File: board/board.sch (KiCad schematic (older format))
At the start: 34 parts, among them P2 POWER, P3 JTAG, U3 LFSPXO025560

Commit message: Schematics and Start of Board Layout
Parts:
- removed C36, C37, C38, C39, C40, C41, C42, C43: 100nF, Capacitors_SMD:C_0805_HandSoldering, symbol C_Small
- removed P3: JTAG, Pin_Headers:Pin_Header_Straight_2x05_Pitch2.54mm, symbol CONN_02X05
- removed U3: LFSPXO025560, Crystals:Crystal_SMD_EuroQuartz_MT-4pin_3.2x2.5mm_HandSoldering, symbol LFSPXO025560
- added AMP1: THS7316, Housings_SOIC:SOIC-8_3.9x4.9mm_Pitch1.27mm, symbol THS7316
- added C1, C2, C3, C4, C5: 10uF, Capacitors_SMD:C_0805_HandSoldering, symbol C_Small
- added GPIO1: CONN_02X17, Pin_Headers:Pin_Header_Straight_2x17_Pitch2.54mm, symbol CONN_02X17
- added JTAG1: CONN_02X05, Pin_Headers:Pin_Header_Straight_2x05_Pitch2.54mm, symbol CONN_02X05
- added L1, L2: 10mH, Capacitors_SMD:C_0805_HandSoldering, symbol L_Small
- added OSC1: XO32050UITA, Oscillators:Oscillator_SMD_EuroQuartz_XO32-4pin_3.2x2.5mm_HandSoldering, symbol XO32050UITA
- added R1, R12, R19: 1k, Resistors_SMD:R_0805_HandSoldering, symbol R_Small
- added R10, R11, R14, R24, R25, R26, R9: 10k, Resistors_SMD:R_0805_HandSoldering, symbol R_Small
- added R13, R20, R3: 2k, Resistors_SMD:R_0805_HandSoldering, symbol R_Small
- added R15, R21, R4: 4k, Resistors_SMD:R_0805_HandSoldering, symbol R_Small
- added R16, R22, R5: 8k, Resistors_SMD:R_0805_HandSoldering, symbol R_Small
- added R17, R23, R6: 16k, Resistors_SMD:R_0805_HandSoldering, symbol R_Small
- added R18, R8: 150, Resistors_SMD:R_0805_HandSoldering, symbol R_Small
- added R27, R28, R29: 75, Resistors_SMD:R_0805_HandSoldering, symbol R_Small
- added R7: 1k1, Resistors_SMD:R_0805_HandSoldering, symbol R_Small
- added RCA1: TrippleRCA, footprints:TrippleRCA, symbol TrippleRCA
- added REG1: LM1117IMPX-3.3, TO_SOT_Packages_SMD:SOT-223, symbol LM1117IMPX-3.3
- C7: value 47u -> 100nF; footprint Capacitors_SMD:C_1206_HandSoldering -> Capacitors_SMD:C_0805_HandSoldering
- POWER1: renamed from P2; value POWER -> CONM_01x02
- R2: value 10k -> 150
- U2: renamed from U?; footprint (none) -> footprints:QFP_144_GND
- renumbered C17 to C11, C18 to C12, C19 to C13, C20 to C14, C21 to C15, C22 to C16, C23 to C17, C24 to C18, C25 to C19, C26 to C20, C27 to C21, C28 to C22, C29 to C23, C30 to C24, C35 to C25, C13 to C6
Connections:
- net labels removed: +5V, 1V8A, 1V8B, 1V8C
- wire segments 87 -> 376
- no-connect marks 3 -> 44
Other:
- note added: "PB"
- note added: "PR"
- note added: "Y"
- moved on the sheet: C6, POWER1, U2

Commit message: Board layout finished
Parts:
- removed GPIO1: CONN_02X17, Pin_Headers:Pin_Header_Straight_2x17_Pitch2.54mm, symbol CONN_02X17
- added C26, C27, C28, C29, C30: 100nF, Capacitors_SMD:C_0603_HandSoldering, symbol C_Small
- added C8: 10uF, Capacitors_SMD:C_0805_HandSoldering, symbol C_Small
- added GPIO1: CONN_02X08, Pin_Headers:Pin_Header_Straight_2x08_Pitch2.54mm, symbol CONN_02X08
- added GPIO2: CONN_02X05, Pin_Headers:Pin_Header_Straight_2x05_Pitch2.54mm, symbol CONN_02X05
- C11, C12, C13, C14, C15, C16, C17, C18, C19, C20, C21, C22, C23, C24, C25, C31, C32, C33, C34, C6, C7: footprint Capacitors_SMD:C_0805_HandSoldering -> Capacitors_SMD:C_0603_HandSoldering
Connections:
- net 3V3A: now also C5.2, C8.2, GPIO1.2 (P2), GPIO2.2 (P2); no longer C5.1, REG1.2 (OUT)
- net 3V3B: now also C26.1, C27.1, C28.1, C29.1, C30.1
- net GND: now also C5.1, C26.2, C27.2, C28.2, C29.2, C30.2, C8.1, GPIO1.1 (P1), GPIO2.1 (P1); no longer C5.2
- net at U2.100 (IO_6): no longer R19.1
- net at U2.101 (IO_6): no longer R20.1
- net at U2.103 (IO_6): no longer R21.1
- net at U2.105 (IO_6): no longer R22.1
- net at U2.106 (IO_6): no longer R23.1
- net at U2.24 (IO_1B): now also GPIO2.3 (P3)
- net at U2.25 (IO_2/CLK0n): now also GPIO2.4 (P4); no longer OSC1.3 (OUT)
- net at U2.26 (IO_2/CLK0p): now also GPIO2.5 (P5)
- net at U2.27 (IO_2/CLK1n): now also GPIO2.6 (P6)
- net at U2.28 (IO_2/CLK1p): now also GPIO2.7 (P7)
- net at U2.31 (IO_2): now also GPIO2.8 (P8)
- net at U2.32 (IO_2/PLL_L_CLKOUTn): now also GPIO2.9 (P9)
- net at U2.33 (IO_2/PLL_L_CLKOUTp): now also GPIO2.10 (P10)
- net at U2.39 (IO_3): now also R1.1
- net at U2.40 (IO_3): now also R3.1
- net at U2.41 (IO_3): now also R4.1
- net at U2.42 (IO_3): now also R5.1
- net at U2.44 (IO_3): now also R6.1
- net at U2.46 (IO_3): now also R7.1
- net at U2.47 (IO_3): now also R12.1
- net at U2.48 (IO_3): now also R13.1
- net at U2.61 (IO_3): now also R15.1
- net at U2.62 (IO_3): now also R16.1
- net at U2.63 (IO_3): now also R17.1
- net at U2.65 (IO_3): now also R19.1
- net at U2.67 (IO_3): now also R20.1
- net at U2.68 (IO_3): now also R21.1
- net at U2.69 (IO_3): now also R22.1
- net at U2.70 (IO_3): now also R23.1
- net at U2.74 (IO_5): now also GPIO1.16 (P16)
- net at U2.75 (IO_5): now also GPIO1.15 (P15)
- net at U2.76 (IO_5): now also GPIO1.14 (P14)
- net at U2.77 (IO_5): now also GPIO1.13 (P13)
- net at U2.78 (IO_5): now also GPIO1.12 (P12); no longer R1.1
- net at U2.79 (IO_5): now also GPIO1.11 (P11); no longer R3.1
- net at U2.80 (IO_5): now also GPIO1.10 (P10)
- net at U2.81 (IO_5): now also GPIO1.9 (P9); no longer R4.1
- net at U2.84 (IO_5): now also GPIO1.8 (P8)
- net at U2.85 (IO_5): now also GPIO1.7 (P7); no longer R5.1
- net at U2.86 (IO_5): now also GPIO1.6 (P6)
- net at U2.87 (IO_5): now also GPIO1.5 (P5); no longer R6.1
- net at U2.88 (IO_6/CLK2p): now also GPIO1.4 (P4)
- net at U2.89 (IO_6/CLK2n): now also GPIO1.3 (P3); no longer R7.1
- net at U2.91 (IO_6/CLK3n): now also OSC1.3 (OUT); no longer R12.1
- net at U2.92 (IO_6): no longer R13.1
- net at U2.95 (IO_6): no longer R15.1
- net at U2.97 (IO_6): no longer R16.1
- net at U2.98 (IO_6): no longer R17.1
- no-connect marks 44 -> 55
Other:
- moved on the sheet: AMP1, C6, C7, OSC1, R1, R12, R13, R15, R16, R17, R18, R19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

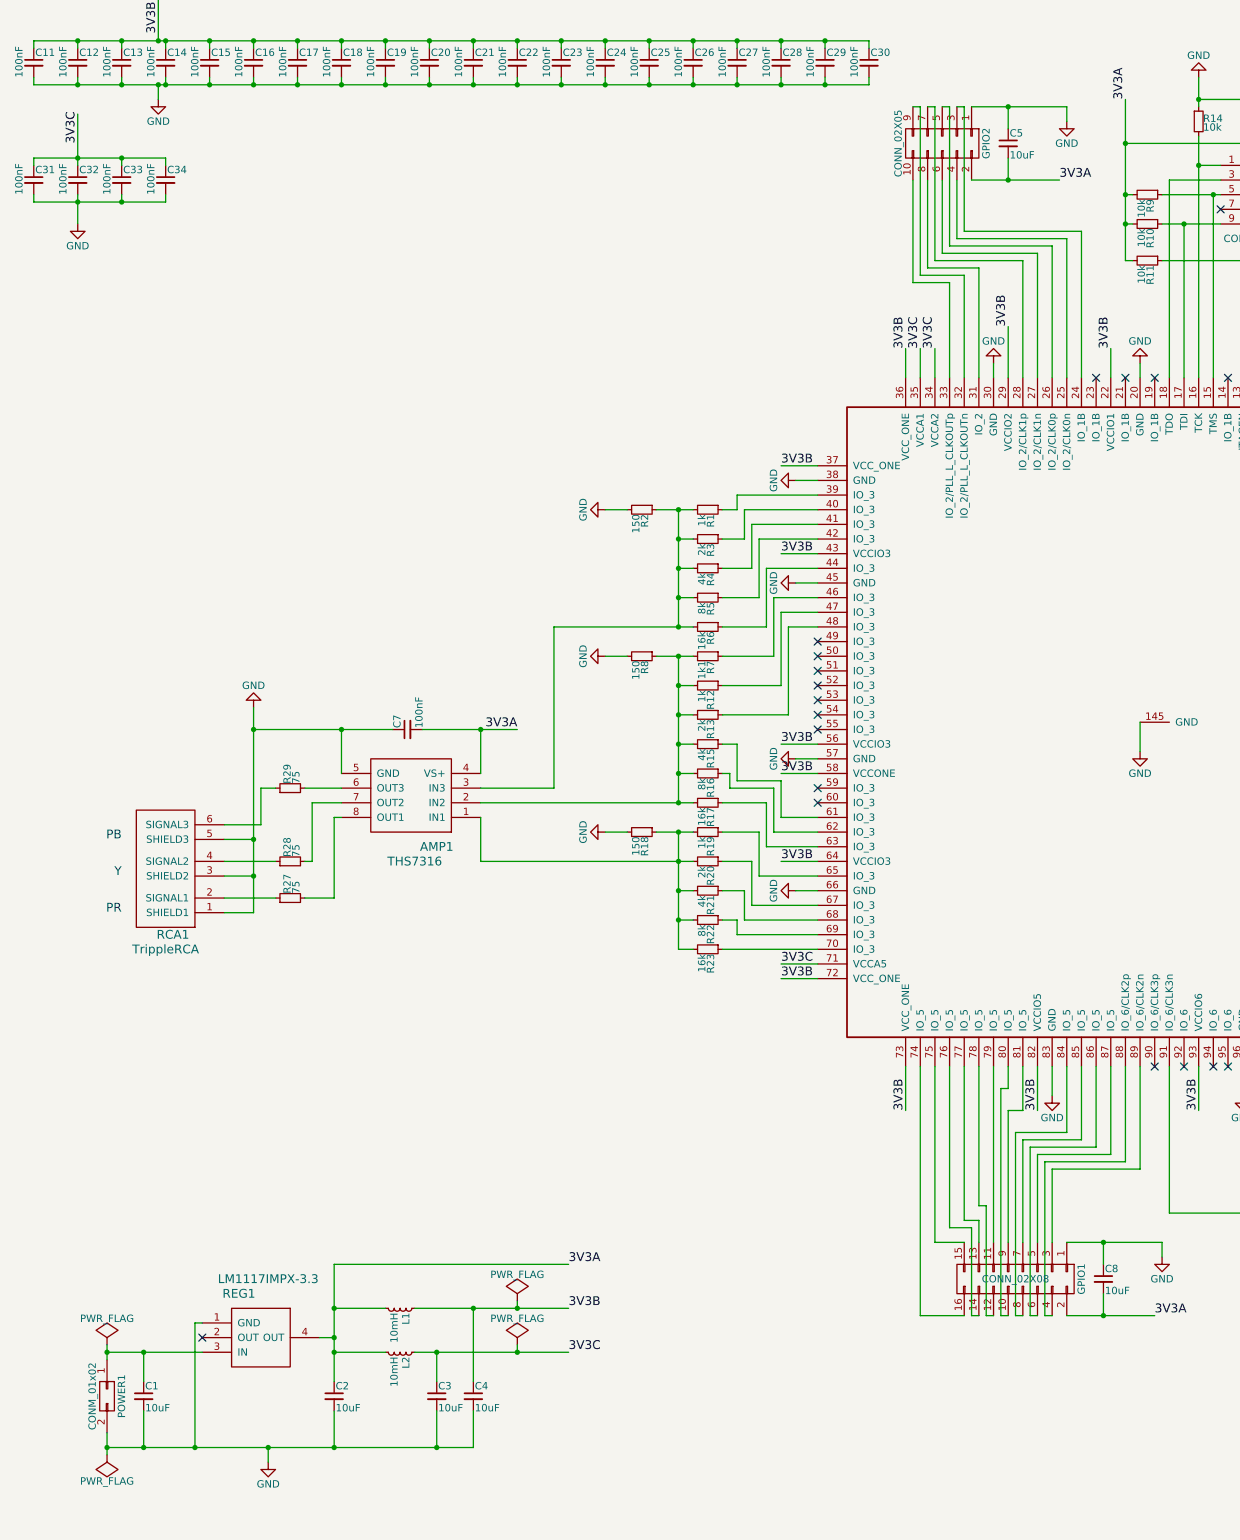
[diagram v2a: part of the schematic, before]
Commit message: Adapter board for ZX Spectrum
Plus some changes to the A-Video board itself to better fit the needs of
the ZX Spectrum mod (which currently drives the development)
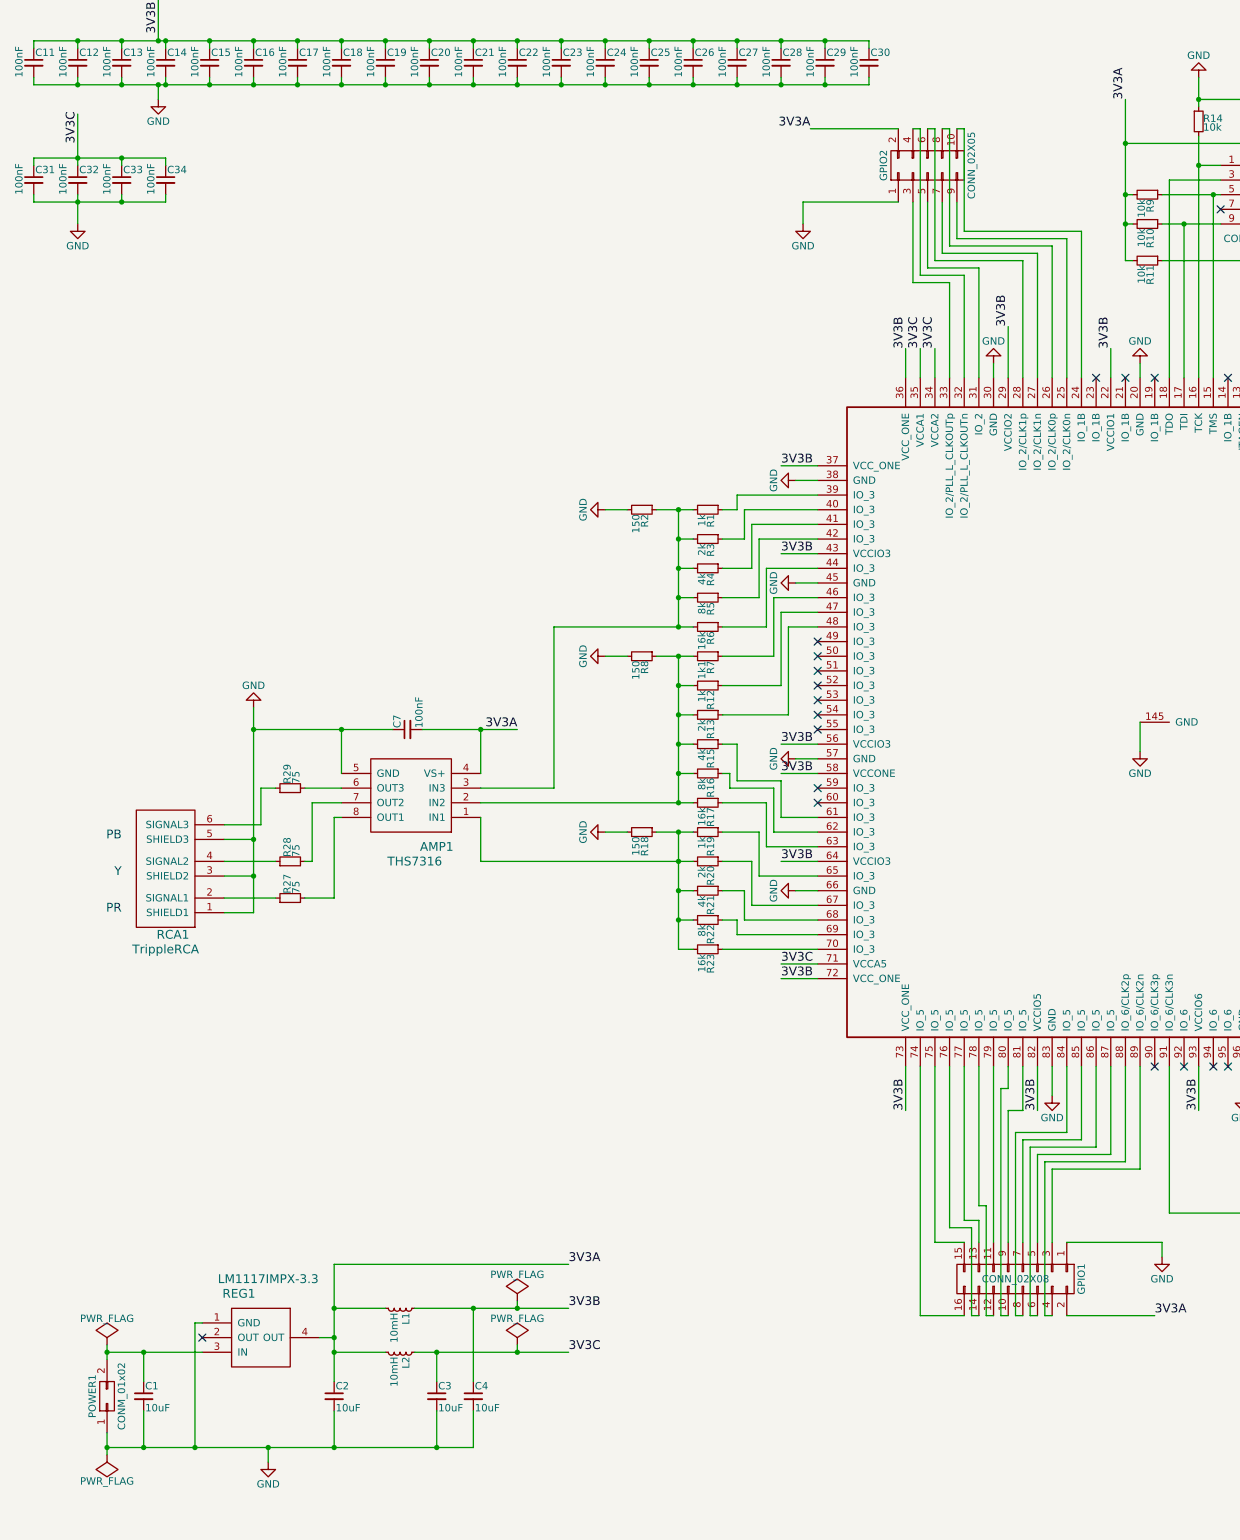
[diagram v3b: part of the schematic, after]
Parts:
- removed C5, C8: 10uF, Capacitors_SMD:C_0805_HandSoldering, symbol C_Small
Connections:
- net GND: now also POWER1.1 (P1); no longer POWER1.2 (P2)
- net at C1.1, REG1.3 (IN): now also POWER1.2 (P2); no longer POWER1.1 (P1)
- net at U2.24 (IO_1B): now also GPIO2.10 (P10); no longer GPIO2.3 (P3)
- net at U2.25 (IO_2/CLK0n): now also GPIO2.9 (P9); no longer GPIO2.4 (P4)
- net at U2.26 (IO_2/CLK0p): now also GPIO2.8 (P8); no longer GPIO2.5 (P5)
- net at U2.27 (IO_2/CLK1n): now also GPIO2.7 (P7); no longer GPIO2.6 (P6)
- net at U2.28 (IO_2/CLK1p): now also GPIO2.6 (P6); no longer GPIO2.7 (P7)
- net at U2.31 (IO_2): now also GPIO2.5 (P5); no longer GPIO2.8 (P8)
- net at U2.32 (IO_2/PLL_L_CLKOUTn): now also GPIO2.4 (P4); no longer GPIO2.9 (P9)
- net at U2.33 (IO_2/PLL_L_CLKOUTp): now also GPIO2.3 (P3); no longer GPIO2.10 (P10)
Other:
- moved on the sheet: GPIO2
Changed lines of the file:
@@
 F 3 "" H 1200 8900 50  0000 C CNN
 	1    1200 10100
-	0    1    1    0
+	0    -1   -1   0
 $EndComp
 $Comp
@@
 	0    1    1    0
 $EndComp
-$Comp
-L C_Small C8
-U 1 1 59EB0B1F
-P 8000 9300
-F 0 "C8" H 8010 9370 50  0000 L CNN
-F 1 "10uF" H 8010 9220 50  0000 L CNN
-F 2 "Capacitors_SMD:C_0805_HandSoldering" H 8000 9300 50  0001 C CNN
-F 3 "" H 8000 9300 50  0000 C CNN
-	1    8000 9300
-	1    0    0    -1
-$EndComp
 Text Label 8350 9550 0    60   ~ 0
 3V3A
@@
 	7750 9050 8400 9050
 Wire Wire Line
-	8000 9200 8000 9050
-Connection ~ 8000 9050
-Wire Wire Line
 	7750 9550 8350 9550
 Wire Wire Line
 	8400 9050 8400 9150
-Wire Wire Line
-	8000 9400 8000 9550
-Connection ~ 8000 9550
 Wire Wire Line
 	6750 9550 7050 9550
@@
 L CONN_02X05 GPIO2
 U 1 1 59EBB195
-P 6900 1550
-F 0 "GPIO2" H 6900 1850 50  0000 C CNN
-F 1 "CONN_02X05" H 6900 1250 50  0000 C CNN
-F 2 "Pin_Headers:Pin_Header_Straight_2x05_Pitch2.54mm" H 6900 350 50  0001 C CNN
-F 3 "" H 6900 350 50  0000 C CNN
-	1    6900 1550
-	0    1    1    0
+P 6800 1700
+F 0 "GPIO2" H 6800 2000 50  0000 C CNN
+F 1 "CONN_02X05" H 6800 1400 50  0000 C CNN
+F 2 "Pin_Headers:Pin_Header_Straight_2x05_Pitch2.54mm" H 6800 500 50  0001 C CNN
+F 3 "" H 6800 500 50  0000 C CNN
+	1    6800 1700
+	0    -1   -1   0
 $EndComp
 NoConn ~ 8350 7850
@@
 NoConn ~ 9850 7850
 NoConn ~ 9950 7850
-$Comp
-L C_Small C5
-U 1 1 59EC1E6D
-P 7350 1550
-F 0 "C5" H 7360 1620 50  0000 L CNN
-F 1 "10uF" H 7360 1470 50  0000 L CNN
-F 2 "Capacitors_SMD:C_0805_HandSoldering" H 7350 1550 50  0001 C CNN
-F 3 "" H 7350 1550 50  0000 C CNN
-	1    7350 1550
-	1    0    0    -1
-$EndComp
-Text Label 7700 1800 0    60   ~ 0
+Text Label 6000 1450 2    60   ~ 0
 3V3A
 $Comp
 L GND #PWR031
 U 1 1 59EC1E74
-P 7750 1400
-F 0 "#PWR031" H 7750 1150 50  0001 C CNN
-F 1 "GND" H 7750 1250 50  0000 C CNN
-F 2 "" H 7750 1400 50  0000 C CNN
-F 3 "" H 7750 1400 50  0000 C CNN
-	1    7750 1400
-	1    0    0    -1
-$EndComp
-Wire Wire Line
-	7100 1300 7750 1300
-Wire Wire Line
-	7350 1450 7350 1300
-Connection ~ 7350 1300
-Wire Wire Line
-	7100 1800 7700 1800
-Wire Wire Line
-	7750 1300 7750 1400
-Wire Wire Line
-	7350 1650 7350 1800
-Connection ~ 7350 1800
+P 5950 2100
+F 0 "#PWR031" H 5950 1850 50  0001 C CNN
+F 1 "GND" H 5950 1950 50  0000 C CNN
+F 2 "" H 5950 2100 50  0000 C CNN
+F 3 "" H 5950 2100 50  0000 C CNN
+	1    5950 2100
+	1    0    0    -1
+$EndComp
+Wire Wire Line
+	5950 1950 6600 1950
+Wire Wire Line
+	6000 1450 6600 1450
 Wire Wire Line
 	6950 2500 6700 2500
 Wire Wire Line
-	6700 2500 6700 1800
+	6700 2500 6700 1950
 Wire Wire Line
 	7050 2450 6750 2450
 Wire Wire Line
-	6750 2450 6750 1300
-Wire Wire Line
-	6750 1300 6700 1300
+	6750 2450 6750 1450
+Wire Wire Line
+	6750 1450 6700 1450
 Wire Wire Line
 	7150 3150 7150 2400
@@
 	7150 2400 6800 2400
 Wire Wire Line
-	6800 2400 6800 1800
+	6800 2400 6800 1950
 Wire Wire Line
 	7450 2350 6850 2350
 Wire Wire Line
-	6850 2350 6850 1300
-Wire Wire Line
-	6850 1300 6800 1300
+	6850 2350 6850 1450
+Wire Wire Line
+	6850 1450 6800 1450
 Wire Wire Line
 	7550 2300 6900 2300
 Wire Wire Line
-	6900 2300 6900 1800
+	6900 2300 6900 1950
 Wire Wire Line
 	7650 3150 7650 2250
@@
 	7650 2250 6950 2250
 Wire Wire Line
-	6950 2250 6950 1300
-Wire Wire Line
-	6950 1300 6900 1300
+	6950 2250 6950 1450
+Wire Wire Line
+	6950 1450 6900 1450
 Wire Wire Line
 	7750 3150 7750 2200
@@
 	7750 2200 7000 2200
 Wire Wire Line
-	7000 2200 7000 1800
+	7000 2200 7000 1950
 Wire Wire Line
 	7850 3150 7850 2150
@@
 	7850 2150 7050 2150
 Wire Wire Line
-	7050 2150 7050 1300
-Wire Wire Line
-	7050 1300 7000 1300
+	7050 2150 7050 1450
+Wire Wire Line
+	7050 1450 7000 1450
 NoConn ~ 6050 5350
 Wire Wire Line
@@
 Connection ~ 6100 850
 Connection ~ 6100 1150
+Wire Wire Line
+	5950 2100 5950 1950
 $EndSCHEMATC

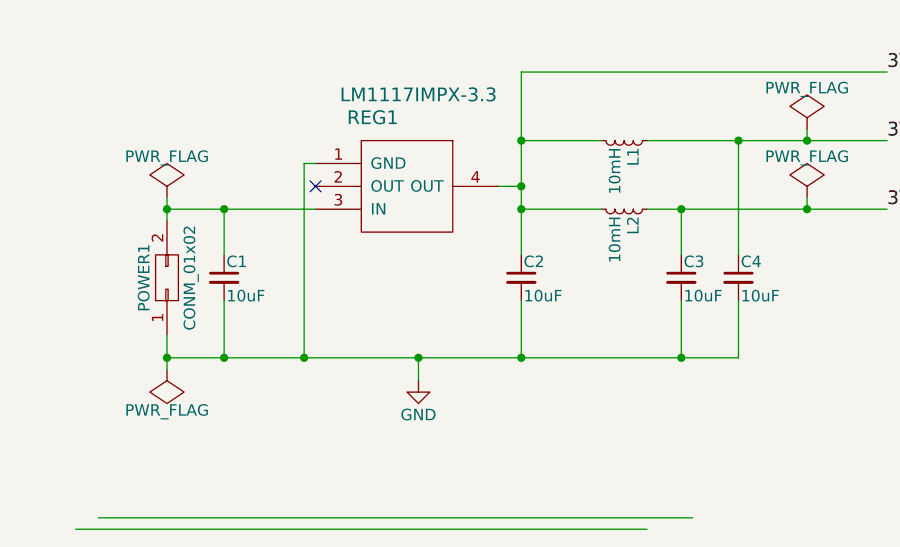
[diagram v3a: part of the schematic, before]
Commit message: small additions for zx spectrum mod
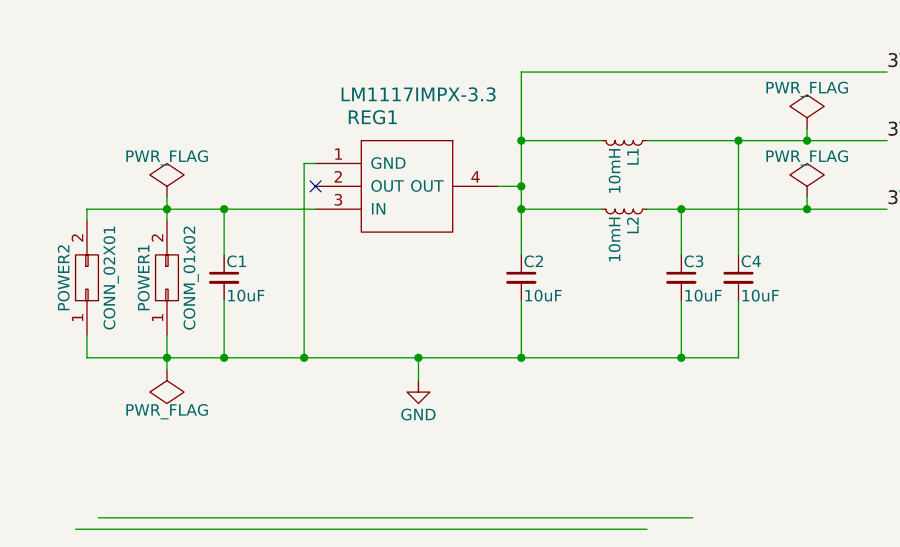
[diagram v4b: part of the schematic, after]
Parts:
- added POWER2: CONN_02X01, Pin_Headers:Pin_Header_Straight_1x02_Pitch2.54mm, symbol CONN_02X01
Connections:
- net GND: now also POWER2.1 (P1)
- net at C1.1, POWER1.2 (P2), REG1.3 (IN): now also POWER2.2 (P2)
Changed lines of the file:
@@
 	1200 10350 1200 10500
 Wire Wire Line
-	1200 10450 3700 10450
+	850  10450 3700 10450
 Connection ~ 1200 10450
 Wire Wire Line
@@
 	2300 10450 2300 10550
 Wire Wire Line
-	1200 9800 1850 9800
+	850  9800 1850 9800
 Wire Wire Line
 	3100 9800 2750 9800
@@
 Wire Wire Line
 	5950 2100 5950 1950
+$Comp
+L CONN_02X01 POWER2
+U 1 1 59F34BAD
+P 850 10100
+F 0 "POWER2" H 850 10200 50  0000 C CNN
+F 1 "CONN_02X01" H 850 10000 50  0000 C CNN
+F 2 "Pin_Headers:Pin_Header_Straight_1x02_Pitch2.54mm" H 850 8900 50  0001 C CNN
+F 3 "" H 850 8900 50  0000 C CNN
+	1    850  10100
+	0    -1   -1   0
+$EndComp
+Wire Wire Line
+	850  9800 850  9850
+Wire Wire Line
+	850  10450 850  10350
 $EndSCHEMATC
